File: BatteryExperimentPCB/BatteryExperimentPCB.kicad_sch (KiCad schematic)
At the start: 30 parts, among them J1 USB_C_Receptacle_USB2.0_14P, J2 Conn_01x11_Pin, J3 Conn_01x11_Pin, Q1 DMG1012T, SW1 SW_Push, U1 ATtiny3226-M, U2 USBLC6-2P6, U3 BQ25628RYKR

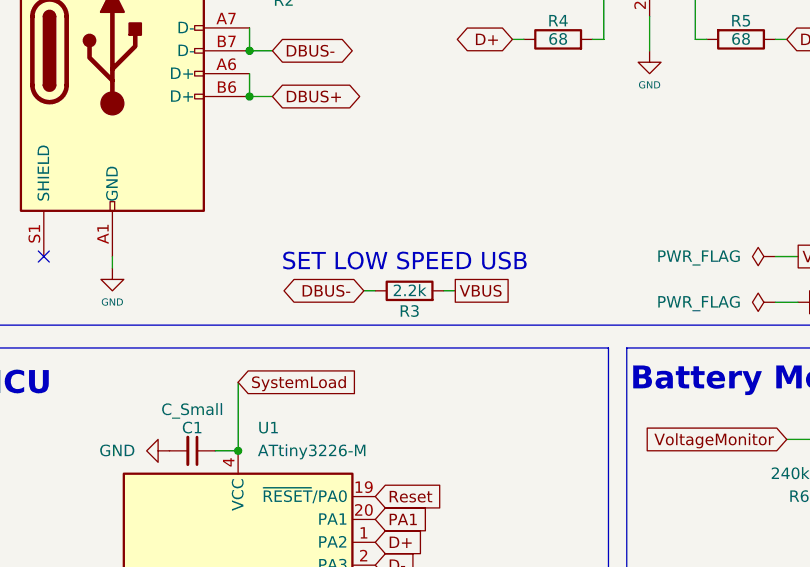
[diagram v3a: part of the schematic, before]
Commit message: get rid of resister for low speed usb
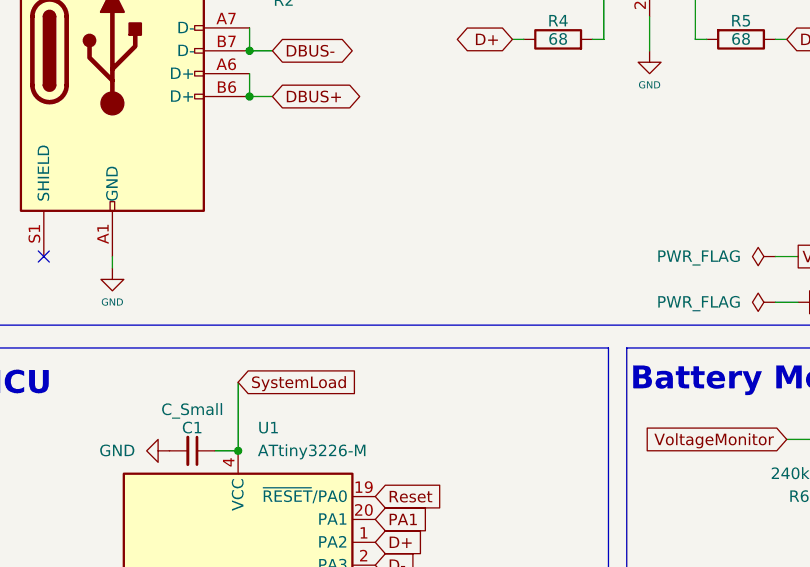
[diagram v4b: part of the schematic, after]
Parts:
- removed R3: 2.2k, Resistor_SMD:R_0201_0603Metric, symbol Device:R
- C1, C2, C3, C4, C5: footprint (none) -> Capacitor_SMD:C_0805_2012Metric
- J2, J3: footprint (none) -> Connector_PinHeader_2.54mm:PinHeader_1x11_P2.54mm_Vertical
- R10, R11, R12, R13, R14, R6, R7, R8, R9: footprint (none) -> Resistor_SMD:R_0805_2012Metric
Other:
- note removed: "SET LOW SPEED USB"
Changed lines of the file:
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@@
 	(wire
 		(pts
-			(xy 58.42 72.39) (xy 59.69 72.39)
-		)
-		(stroke
-			(width 0)
-			(type default)
-		)
-	)
-	(wire
-		(pts
 			(xy 104.14 44.45) (xy 105.41 44.45)
 		)
@@
 	(wire
 		(pts
-			(xy 67.31 72.39) (xy 68.58 72.39)
-		)
-		(stroke
-			(width 0)
-			(type default)
-		)
-	)
-	(wire
-		(pts
 			(xy 110.49 88.9) (xy 110.49 90.17)
 		)
@@
 		)
 	)
-	(text "SET LOW SPEED USB"
-		(exclude_from_sim no)
-		(at 62.992 69.342 0)
-		(effects
-			(font
-				(size 1.905 1.905)
-			)
-		)
-	)
 	(text "BREAKOUT PINS"
 		(exclude_from_sim no)
@@
 		)
 	)
-	(global_label "DBUS-"
-		(shape bidirectional)
-		(at 58.42 72.39 180)
-		(effects
-			(font
-				(size 1.27 1.27)
-			)
-			(justify right)
-		)
-		(property "Intersheetrefs" "${INTERSHEET_REFS}"
-			(at 47.8305 72.4694 0)
-			(effects
-				(font
-					(size 1.27 1.27)
-				)
-				(justify right)
-				(hide yes)
-			)
-		)
-	)
 	(global_label "CaseRed"
 		(shape input)
@@
 		)
 	)
-	(global_label "VBUS"
-		(shape passive)
-		(at 68.58 72.39 0)
-		(effects
-			(font
-				(size 1.27 1.27)
-			)
-			(justify left)
-		)
-		(property "Intersheetrefs" "${INTERSHEET_REFS}"
-			(at -275.59 -236.855 0)
-			(effects
-				(font
-					(size 1.27 1.27)
-				)
-				(hide yes)
-			)
-		)
-	)
 	(global_label "QON"
 		(shape input)
@@
 			)
 		)
-		(property "Footprint" ""
+		(property "Footprint" "Resistor_SMD:R_0805_2012Metric"
 			(at 112.268 93.98 90)
 			(effects
@@
 			)
 		)
-		(property "Footprint" ""
+		(property "Footprint" "Connector_PinHeader_2.54mm:PinHeader_1x11_P2.54mm_Vertical"
 			(at 203.2 106.68 0)
 			(effects
@@
 			)
 		)
-		(property "Footprint" ""
+		(property "Footprint" "Resistor_SMD:R_0805_2012Metric"
 			(at 214.63 40.64 0)
 			(effects
@@
 			)
 		)
-		(property "Footprint" ""
+		(property "Footprint" "Connector_PinHeader_2.54mm:PinHeader_1x11_P2.54mm_Vertical"
 			(at 227.33 106.68 0)
 			(effects
@@
 			)
 		)
-		(property "Footprint" ""
+		(property "Footprint" "Resistor_SMD:R_0805_2012Metric"
 			(at 179.07 106.68 0)
 			(effects
@@
 			)
 		)
-		(property "Footprint" ""
+		(property "Footprint" "Resistor_SMD:R_0805_2012Metric"
 			(at 214.63 72.39 0)
 			(effects
@@
 			)
 		)
-		(property "Footprint" ""
+		(property "Footprint" "Capacitor_SMD:C_0805_2012Metric"
 			(at 176.53 60.96 0)
 			(effects
@@
 			)
 		)
-		(property "Footprint" ""
+		(property "Footprint" "Capacitor_SMD:C_0805_2012Metric"
 			(at 39.37 90.17 0)
 			(effects
@@
 			)
 		)
-		(property "Footprint" ""
+		(property "Footprint" "Capacitor_SMD:C_0805_2012Metric"
 			(at 129.54 35.56 0)
 			(effects
@@
 			)
 		)
-		(property "Footprint" ""
+		(property "Footprint" "Resistor_SMD:R_0805_2012Metric"
 			(at 179.07 96.52 0)
 			(effects
@@
 			)
 		)
-		(property "Footprint" ""
+		(property "Footprint" "Capacitor_SMD:C_0805_2012Metric"
 			(at 135.89 72.39 0)
 			(effects
@@
 			)
 		)
-		(property "Footprint" ""
+		(property "Footprint" "Resistor_SMD:R_0805_2012Metric"
 			(at 214.63 31.75 0)
 			(effects
@@
 			)
 		)
-		(property "Footprint" ""
+		(property "Footprint" "Resistor_SMD:R_0805_2012Metric"
 			(at 116.84 87.122 90)
 			(effects
@@
 			)
 		)
-		(property "Footprint" ""
+		(property "Footprint" "Capacitor_SMD:C_0805_2012Metric"
 			(at 133.35 63.5 0)
 			(effects
@@
 	)
 	(symbol
-		(lib_id "Device:R")
-		(at 63.5 72.39 90)
-		(unit 1)
-		(exclude_from_sim no)
-		(in_bom yes)
-		(on_board yes)
-		(dnp no)
-		(property "Reference" "R3"
-			(at 63.5 74.676 90)
-			(effects
-				(font
-					(size 1.27 1.27)
-				)
-			)
-		)
-		(property "Value" "2.2k"
-			(at 63.5 72.39 90)
-			(effects
-				(font
-					(size 1.27 1.27)
-				)
-			)
-		)
-		(property "Footprint" "Resistor_SMD:R_0201_0603Metric"
-			(at 63.5 74.168 90)
-			(effects
-				(font
-					(size 1.27 1.27)
-				)
-				(hide yes)
-			)
-		)
-		(property "Datasheet" "~"
-			(at 63.5 72.39 0)
-			(effects
-				(font
-					(size 1.27 1.27)
-				)
-				(hide yes)
-			)
-		)
-		(property "Description" "Resistor"
-			(at 63.5 72.39 0)
-			(effects
-				(font
-					(size 1.27 1.27)
-				)
-				(hide yes)
-			)
-		)
-		(pin "1"
-		)
-		(pin "2"
-		)
-		(instances
-			(project "BatteryExperimentPCB"
-				(path "/057a57c5-fa69-4f68-8ff5-75480ccd2fb3"
-					(reference "R3")
-					(unit 1)
-				)
-			)
-		)
-	)
-	(symbol
 		(lib_id "power:GND")
 		(at 232.41 114.3 90)
@@
 			)
 		)
-		(property "Footprint" ""
+		(property "Footprint" "Resistor_SMD:R_0805_2012Metric"
 			(at 179.07 101.6 0)
 			(effects
@@
 			)
 		)
-		(property "Footprint" ""
+		(property "Footprint" "Resistor_SMD:R_0805_2012Metric"
 			(at 214.63 22.86 0)
 			(effects

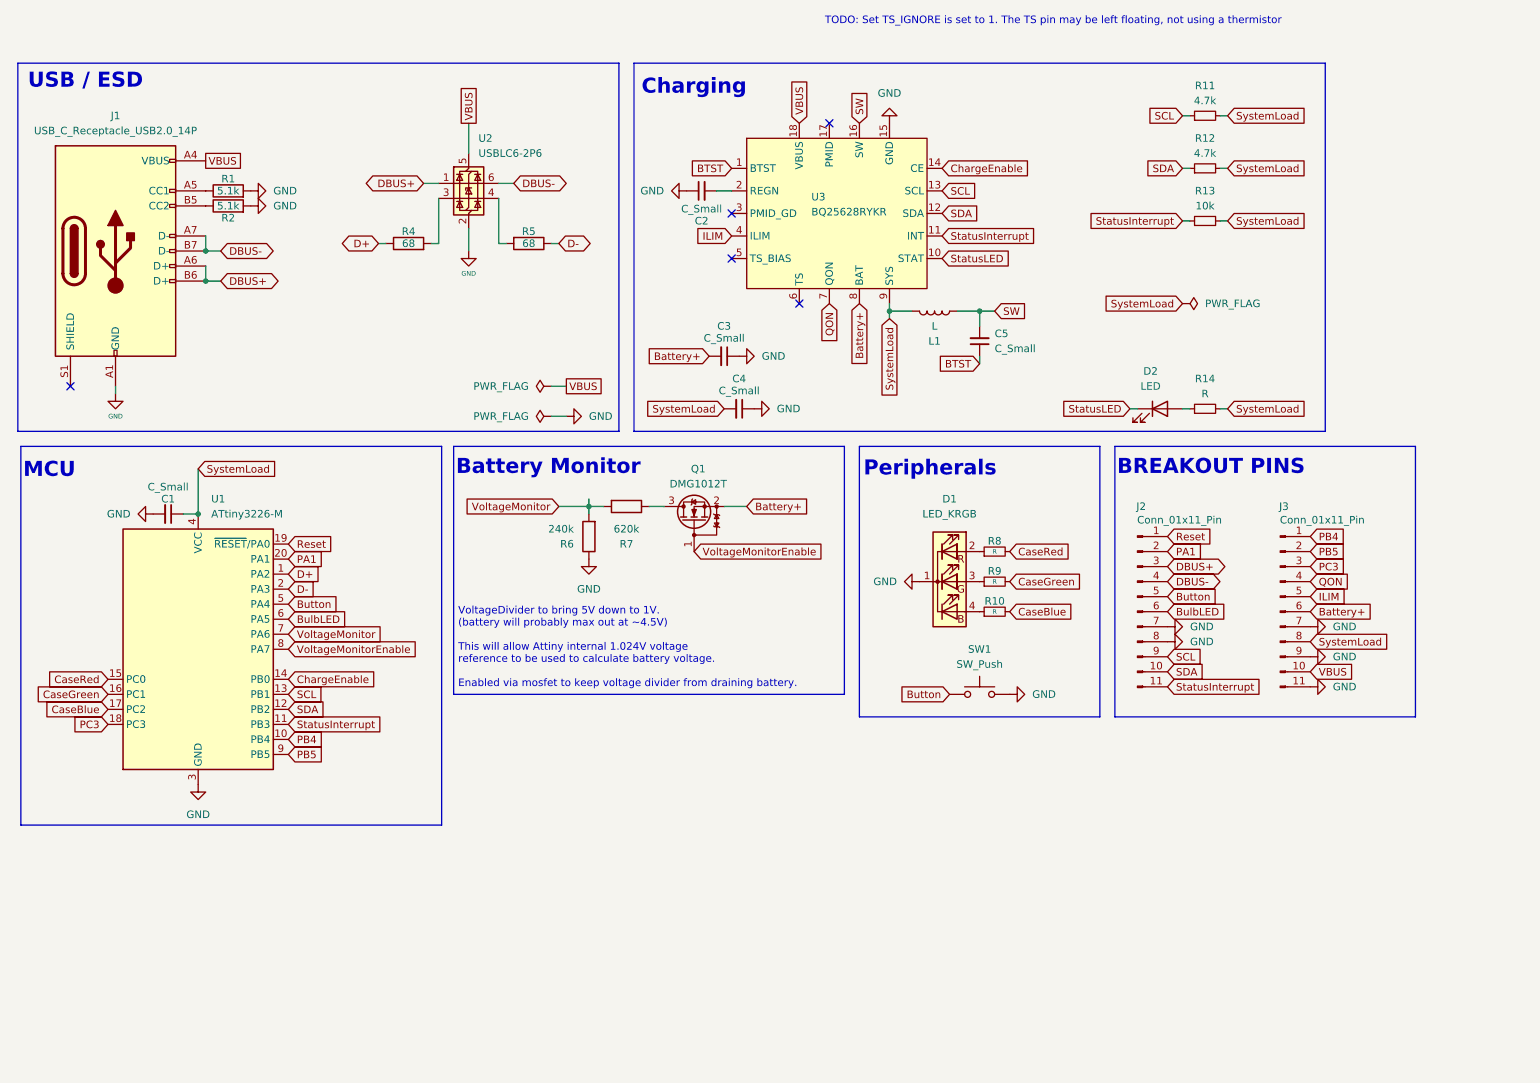
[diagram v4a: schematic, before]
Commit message: add low speed resistor back
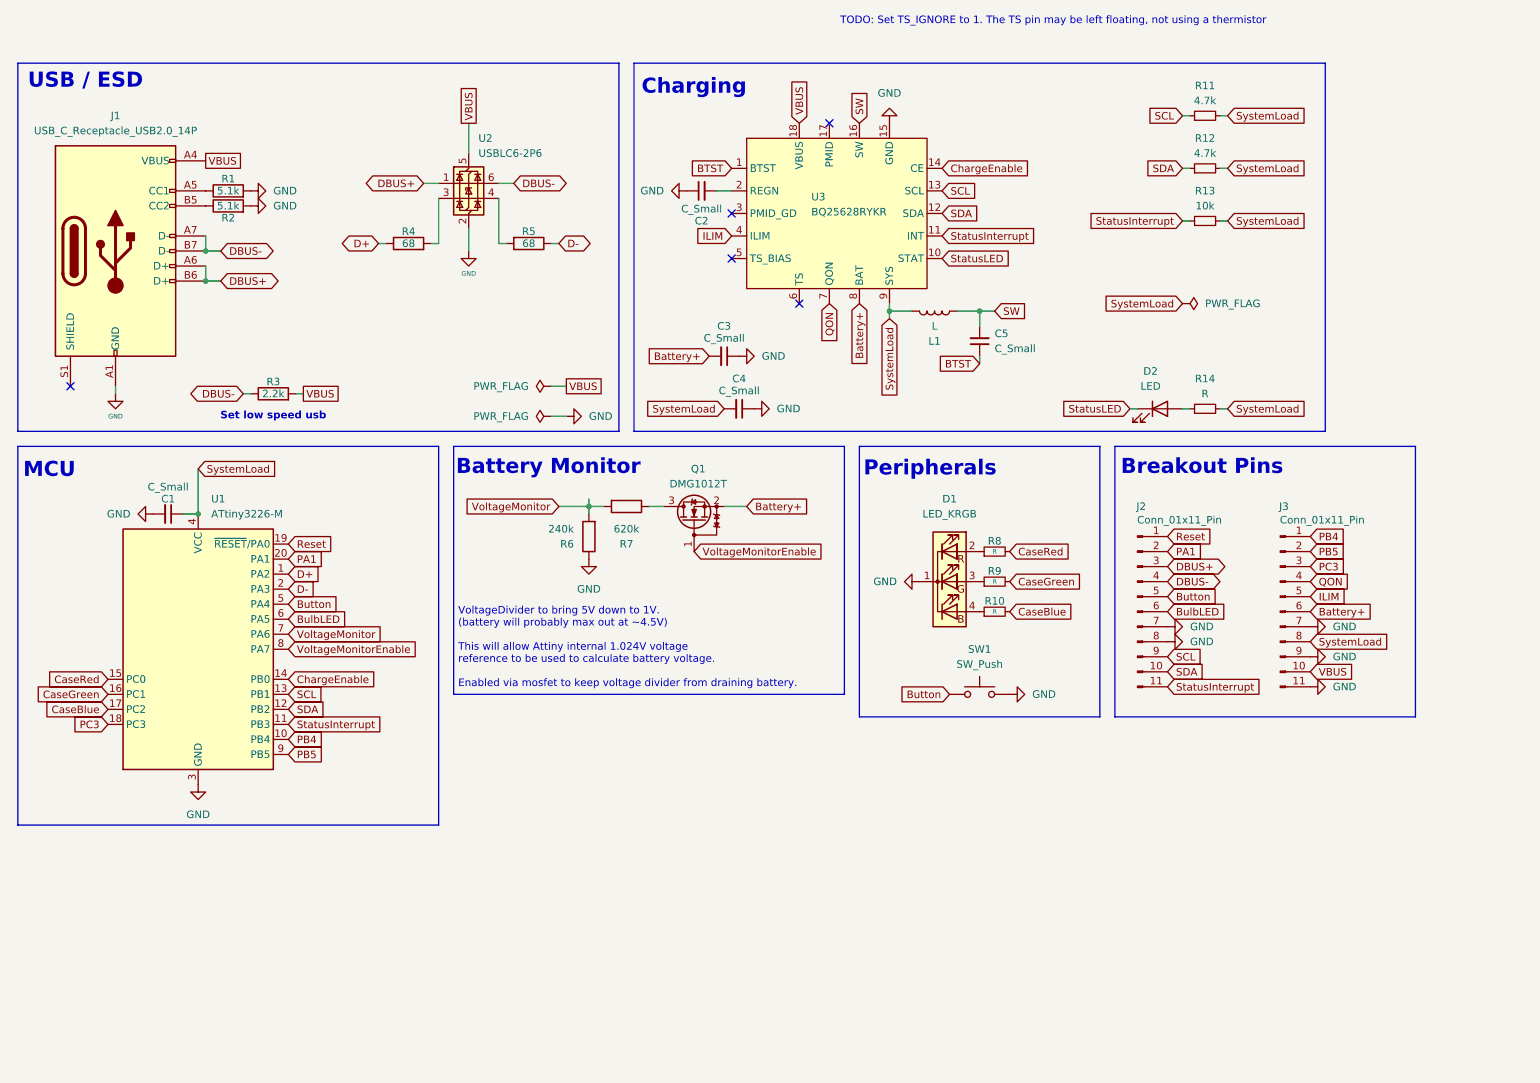
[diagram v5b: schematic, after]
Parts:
- added R3: 2.2k, symbol Device:R
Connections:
- net DBUS-: now also R3.1
- net VBUS: now also R3.2
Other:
- note added: "Breakout Pins"
- note added: "Set low speed usb"
- note added: "TODO: Set TS_IGNORE to 1. The TS pin may be left floating, not using a thermistor"
- note removed: "BREAKOUT PINS"
- note removed: "TODO: Set TS_IGNORE is set to 1. The TS pin may be left floating, not using a thermistor"
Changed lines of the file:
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@@
+	(wire
+		(pts
+			(xy 52.07 69.85) (xy 53.34 69.85)
+		)
+		(stroke
+			(width 0)
+			(type default)
+		)
+	)
 	(wire
 		(pts
@@
 		(pts
 			(xy 110.49 87.63) (xy 110.49 88.9)
+		)
+		(stroke
+			(width 0)
+			(type default)
+		)
+	)
+	(wire
+		(pts
+			(xy 60.96 69.85) (xy 62.23 69.85)
 		)
 		(stroke
@@
 	)
 	(rectangle
-		(start 14.478 78.74)
-		(end 85.598 142.748)
+		(start 13.97 78.74)
+		(end 85.09 142.748)
 		(stroke
 			(width 0)
@@
 		)
 	)
-	(text "TODO: Set TS_IGNORE is set to 1. The TS pin may be left floating, not using a thermistor"
+	(text "Set low speed usb"
+		(exclude_from_sim no)
+		(at 57.15 73.66 0)
+		(effects
+			(font
+				(size 1.27 1.27)
+				(bold yes)
+			)
+		)
+	)
+	(text "TODO: Set TS_IGNORE to 1. The TS pin may be left floating, not using a thermistor"
 		(exclude_from_sim no)
 		(at 188.976 6.858 0)
@@
 		)
 	)
-	(text "BREAKOUT PINS"
+	(text "Breakout Pins"
 		(exclude_from_sim no)
-		(at 215.646 82.296 0)
+		(at 214.122 82.296 0)
 		(effects
 			(font
@@
 		)
 	)
+	(global_label "DBUS-"
+		(shape bidirectional)
+		(at 52.07 69.85 180)
+		(effects
+			(font
+				(size 1.27 1.27)
+			)
+			(justify right)
+		)
+		(property "Intersheetrefs" "${INTERSHEET_REFS}"
+			(at 41.4805 69.9294 0)
+			(effects
+				(font
+					(size 1.27 1.27)
+				)
+				(justify right)
+				(hide yes)
+			)
+		)
+	)
 	(global_label "Reset"
 		(shape input)
@@
 		(property "Intersheetrefs" "${INTERSHEET_REFS}"
 			(at -298.45 -278.765 0)
+			(effects
+				(font
+					(size 1.27 1.27)
+				)
+				(hide yes)
+			)
+		)
+	)
+	(global_label "VBUS"
+		(shape passive)
+		(at 62.23 69.85 0)
+		(effects
+			(font
+				(size 1.27 1.27)
+			)
+			(justify left)
+		)
+		(property "Intersheetrefs" "${INTERSHEET_REFS}"
+			(at -281.94 -239.395 0)
 			(effects
 				(font
@@
 					(unit 1)
 				)
+			)
+		)
+	)
+	(symbol
+		(lib_id "Device:R")
+		(at 57.15 69.85 90)
+		(unit 1)
+		(exclude_from_sim no)
+		(in_bom yes)
+		(on_board yes)
+		(dnp no)
+		(property "Reference" "R3"
+			(at 57.15 67.818 90)
+			(effects
+				(font
+					(size 1.27 1.27)
+				)
+			)
+		)
+		(property "Value" "2.2k"
+			(at 57.15 69.85 90)
+			(effects
+				(font
+					(size 1.27 1.27)
+				)
+			)
+		)
+		(property "Footprint" ""
+			(at 57.15 71.628 90)
+			(effects
+				(font
+					(size 1.27 1.27)
+				)
+				(hide yes)
+			)
+		)
+		(property "Datasheet" "~"
+			(at 57.15 69.85 0)
+			(effects
+				(font
+					(size 1.27 1.27)
+				)
+				(hide yes)
+			)
+		)
+		(property "Description" "Resistor"
+			(at 57.15 69.85 0)
+			(effects
+				(font
+					(size 1.27 1.27)
+				)
+				(hide yes)
+			)
+		)
+		(pin "2"
+		)
+		(pin "1"
+		)
+		(instances
+			(project ""
+				(path "/057a57c5-fa69-4f68-8ff5-75480ccd2fb3"
+					(reference "R3")
+					(unit 1)
+				)

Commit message: adding values for resisters and capacitors, added more decoupling capacitors
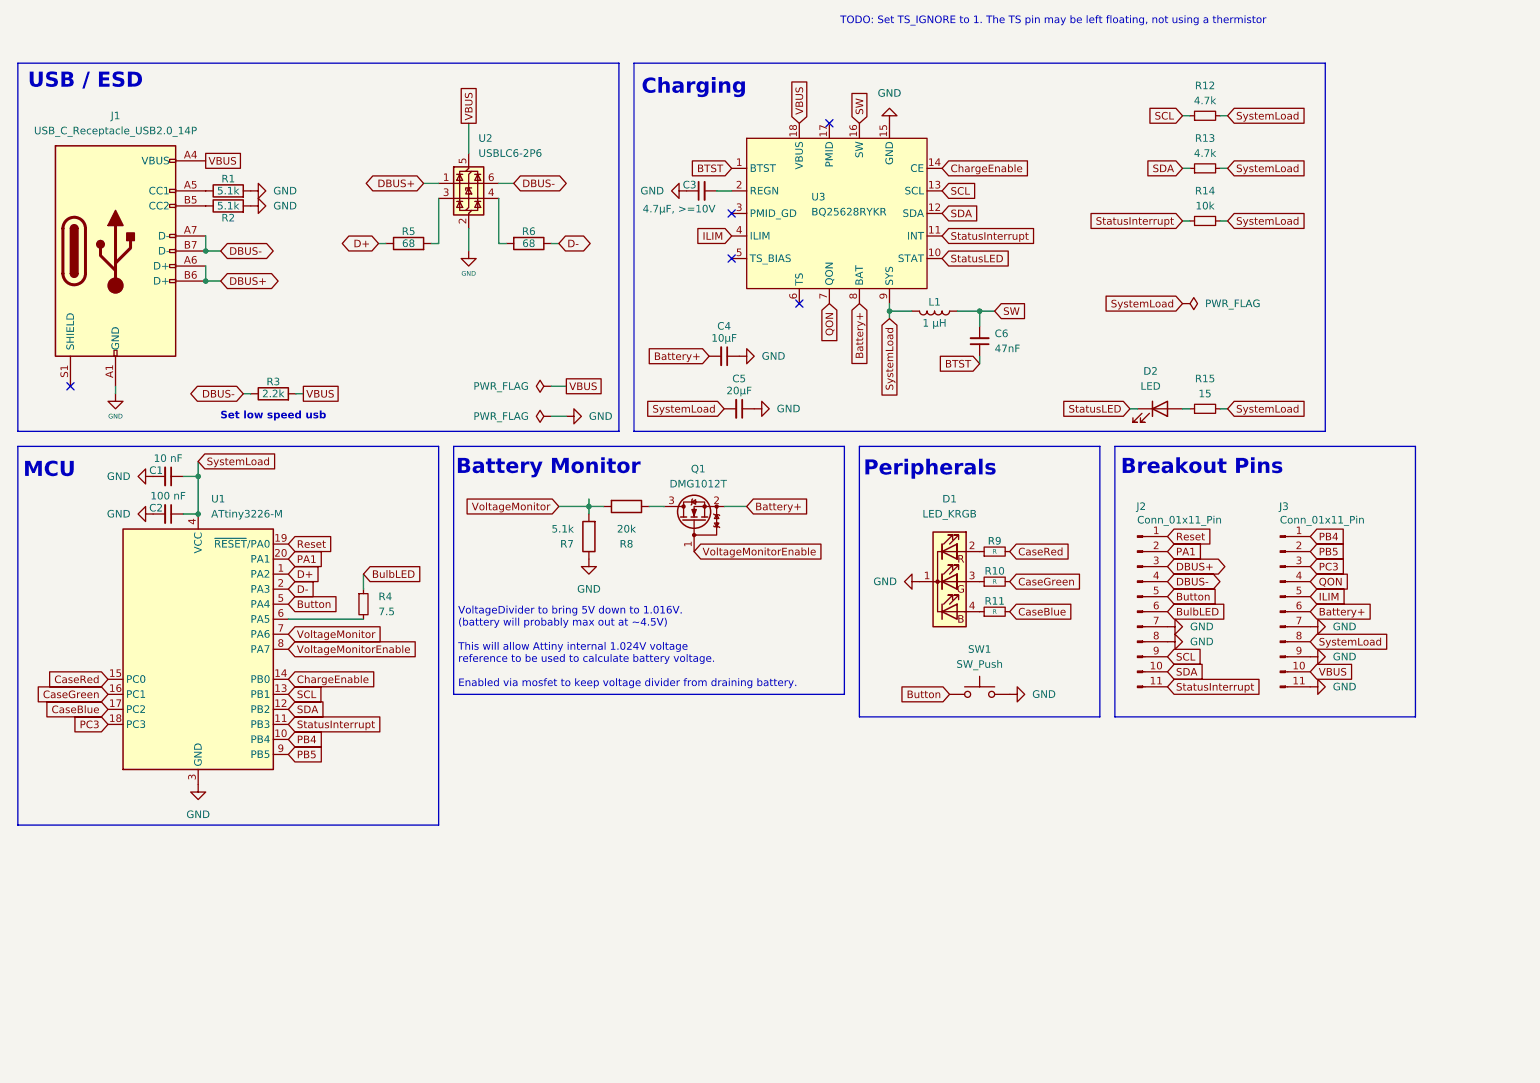
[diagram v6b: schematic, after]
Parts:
- added C1: 10 nF, Capacitor_SMD:C_0805_2012Metric, symbol Device:C_Small
- added R4: 7.5, Resistor_SMD:R_0805_2012Metric, symbol Device:R_Small
- C2: renamed from C1; value C_Small -> 100 nF
- C3: renamed from C2; value C_Small -> 4.7μF, >=10V
- C4: renamed from C3; value C_Small -> 10μF
- C5: renamed from C4; value C_Small -> 20μF
- C6: renamed from C5; value C_Small -> 47nF
- L1: value L -> 1 μH
- R1, R2: footprint Resistor_SMD:R_0201_0603Metric -> Resistor_SMD:R_0805_2012Metric
- R15: renamed from R14; value R -> 15
- R3, SW1, U3: footprint (none) -> Resistor_SMD:R_0805_2012Metric
- R5: renamed from R4; footprint Resistor_SMD:R_0201_0603Metric -> Resistor_SMD:R_0805_2012Metric
- R6: renamed from R5; footprint Resistor_SMD:R_0201_0603Metric -> Resistor_SMD:R_0805_2012Metric
- R7: renamed from R6; value 240k -> 5.1k
- R8: renamed from R7; value 620k -> 20k
- renumbered R9 to R10, R10 to R11, R11 to R12, R12 to R13, R13 to R14, R8 to R9
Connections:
- net BulbLED: now also R4.1; no longer U1.6 (PA5)
- net GND: now also C1.2
- net SystemLoad: now also C1.1
- new net: R4.2, U1.6 (PA5)
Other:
- note added: "VoltageDivider to bring 5V down to 1.016V. (battery will probably max out at ~4.5V) This will allow Attiny internal 1.024V voltage reference to be used to calculate battery voltage. Enabled via mosfet to keep voltage divider from draining battery."
- note removed: "VoltageDivider to bring 5V down to 1V. (battery will probably max out at ~4.5V) This will allow Attiny internal 1.024V voltage reference to be used to calculate battery voltage. Enabled via mosfet to keep voltage divider from draining battery."
